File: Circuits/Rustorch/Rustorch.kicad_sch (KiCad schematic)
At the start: 57 parts, among them CN1 USB_C_Receptacle_USB2.0_16P, CN2 OLED_128x64_IIC, Q1 2SC1815, Q2 2SC1815, Q3 2SC1815, Q4 2SC1815, SW1 RESET, SW2 SW_UP, SW3 SW_LEFT, SW4 SW_RIGHT, SW5 SW_DOWN, SW6 SW_A, SW7 SW_B, SW8 SW_BOOT, SW9 SW_POWER (5P), U1 ESP32-C6-WROOM-1, U2 BA033CC0T, U3 OSL10561-L*, U4 OSL10561-L*, U5 OSL10561-L*, U6 OSL10561-L*

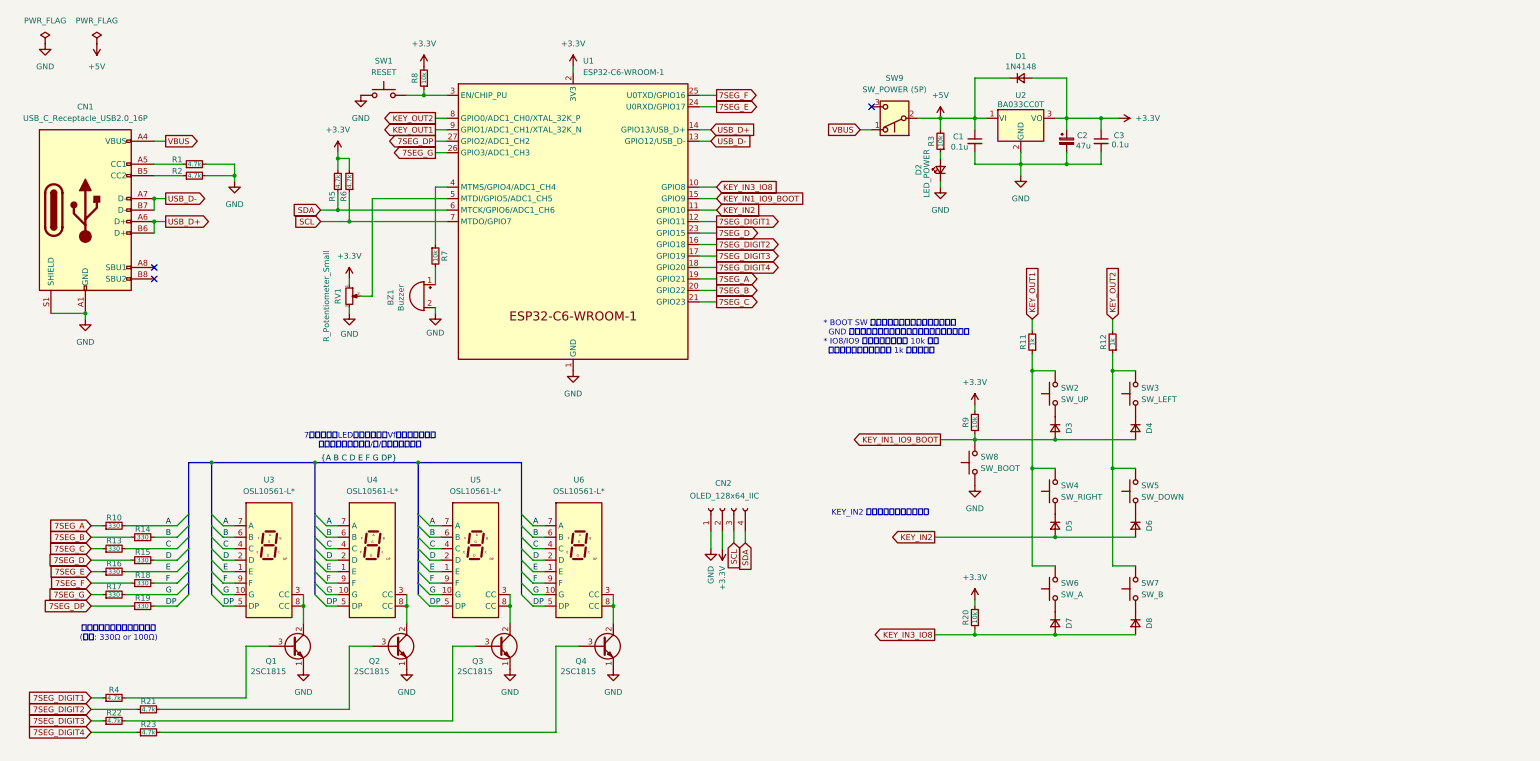
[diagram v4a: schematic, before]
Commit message: (Rustorch) 回路図修正 (部品番号の振り直し)
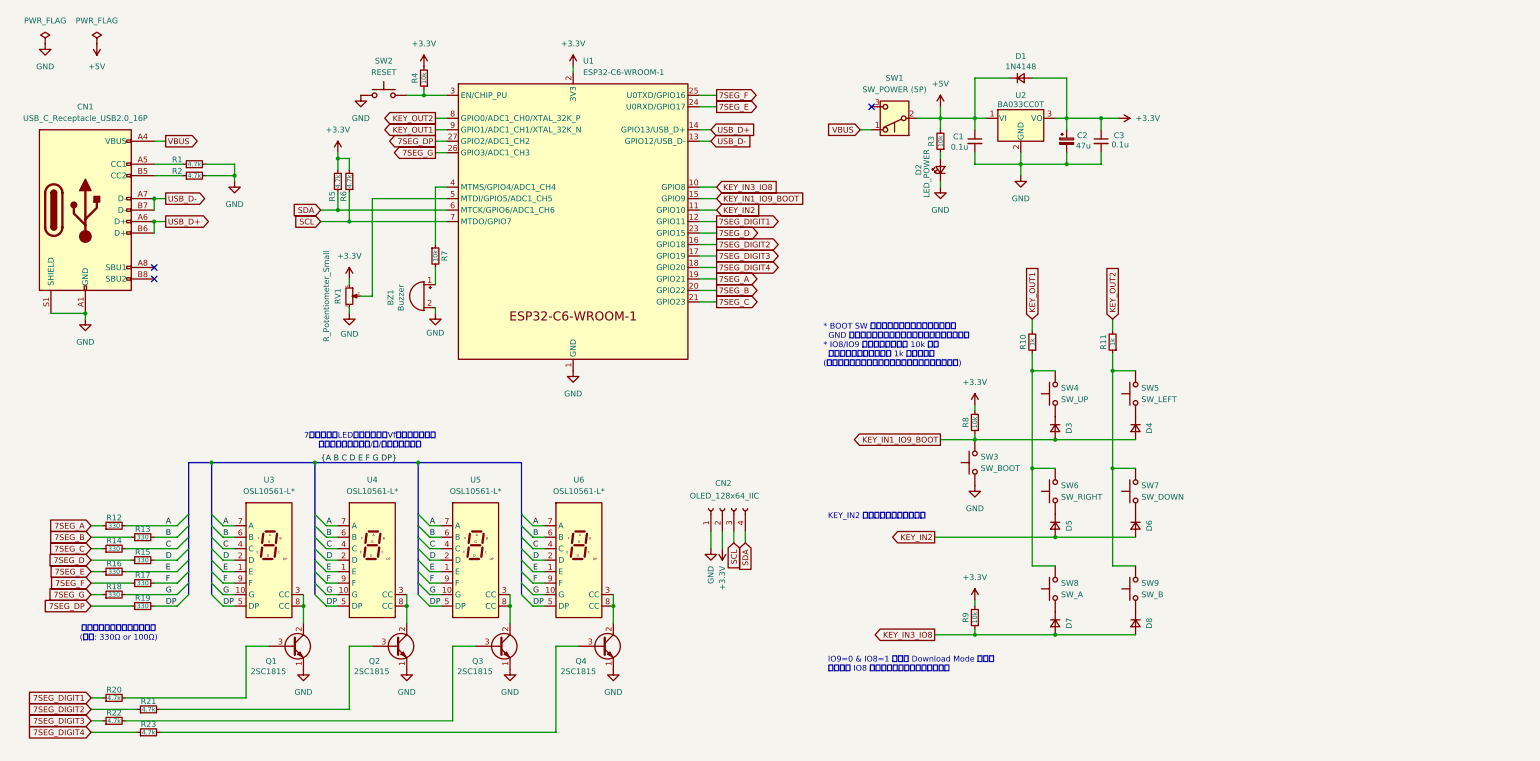
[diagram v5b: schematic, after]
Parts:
- renumbered R11 to R10, R12 to R11, R10 to R12, R14 to R13, R13 to R14, R18 to R17, R17 to R18, R4 to R20, R8 to R4, R9 to R8, R20 to R9, SW9 to SW1, SW1 to SW2, SW8 to SW3, SW2 to SW4, SW3 to SW5, SW4 to SW6, SW5 to SW7, SW6 to SW8, SW7 to SW9
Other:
- note added: "* BOOT SW 押下時にキースキャン用の出力が GND 直結になるのを防止する用に直列抵抗を入れる * IO8/IO9 のプルアップ抵抗 10k との 分圧を考えて直列抵抗は 1k にしておく (ダイオードがあるので不要かもしれないが念のため)"
- note added: "IO9=0 & IO8=1 の時に Download Mode になる このため IO8 にプルアップ抵抗を入れておく"
- note removed: "* BOOT SW 押下時にキースキャン用の出力が GND 直結になるのを防止する用に直列抵抗を入れる * IO8/IO9 のプルアップ抵抗 10k との 分圧を考えて直列抵抗は 1k にしておく"
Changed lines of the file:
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@@
 	(wire
 		(pts
+			(xy 224.79 39.37) (xy 224.79 41.91)
+		)
+		(stroke
+			(width 0)
+			(type default)
+		)
+	)
+	(wire
+		(pts
 			(xy 250.19 41.91) (xy 252.73 41.91)
 		)
@@
 	(text "KEY_IN2 は内蔵プルアップを使用"
 		(exclude_from_sim no)
-		(at 200.66 129.286 0)
+		(at 199.898 130.048 0)
+		(effects
+			(font
+				(face "Meiryo UI")
+				(size 1.27 1.27)
+			)
+			(justify left)
+		)
+	)
+	(text "IO9=0 & IO8=1 の時に Download Mode になる\nこのため IO8 にプルアップ抵抗を入れておく"
+		(exclude_from_sim no)
+		(at 199.898 162.814 0)
 		(effects
 			(font
@@
 		)
 	)
-	(text "* BOOT SW 押下時にキースキャン用の出力が\n  GND 直結になるのを防止する用に直列抵抗を入れる\n* IO8/IO9 のプルアップ抵抗 10k との\n  分圧を考えて直列抵抗は 1k にしておく"
+	(text "* BOOT SW 押下時にキースキャン用の出力が\n  GND 直結になるのを防止する用に直列抵抗を入れる\n* IO8/IO9 のプルアップ抵抗 10k との\n  分圧を考えて直列抵抗は 1k にしておく\n(ダイオードがあるので不要かもしれないが念のため)"
 		(exclude_from_sim no)
-		(at 198.882 90.424 0)
+		(at 198.882 92.202 0)
 		(effects
 			(font
@@
 	(symbol
 		(lib_id "power:+5V")
-		(at 224.79 41.91 0)
+		(at 224.79 39.37 0)
 		(unit 1)
 		(exclude_from_sim no)
@@
 		(fields_autoplaced yes)
 		(property "Reference" "#PWR020"
-			(at 224.79 45.72 0)
+			(at 224.79 43.18 0)
 			(effects
 				(font
@@
 		)
 		(property "Value" "+5V"
-			(at 224.79 36.83 0)
+			(at 224.79 34.29 0)
 			(effects
 				(font
@@
 		)
 		(property "Footprint" ""
-			(at 224.79 41.91 0)
+			(at 224.79 39.37 0)
 			(effects
 				(font
@@
 		)
 		(property "Datasheet" ""
-			(at 224.79 41.91 0)
+			(at 224.79 39.37 0)
 			(effects
 				(font
@@
 		)
 		(property "Description" "Power symbol creates a global label with name \"+5V\""
-			(at 224.79 41.91 0)
+			(at 224.79 39.37 0)
 			(effects
 				(font
@@
 		(on_board yes)
 		(dnp no)
-		(property "Reference" "R12"
+		(property "Reference" "R11"
 			(at 260.858 91.44 90)
 			(effects
@@
 			(project "Rustorch"
 				(path "/3b188497-bb0d-4776-a9fa-7cb2b780d2ff"
-					(reference "R12")
+					(reference "R11")
 					(unit 1)
 				)
@@
 		(dnp no)
 		(fields_autoplaced yes)
-		(property "Reference" "SW9"
+		(property "Reference" "SW1"
 			(at 214.63 33.02 0)
 			(effects
@@
 			(project ""
 				(path "/3b188497-bb0d-4776-a9fa-7cb2b780d2ff"
-					(reference "SW9")
+					(reference "SW1")
 					(unit 1)
 				)
@@
 		(on_board yes)
 		(dnp no)
-		(property "Reference" "R17"
+		(property "Reference" "R18"
 			(at 41.91 145.542 90)
 			(effects
@@
 			(project "Rustorch"
 				(path "/3b188497-bb0d-4776-a9fa-7cb2b780d2ff"
-					(reference "R17")
+					(reference "R18")
 					(unit 1)
 				)
@@
 		(on_board yes)
 		(dnp no)
-		(property "Reference" "R18"
+		(property "Reference" "R17"
 			(at 48.26 143.002 90)
 			(effects
@@
 			(project "Rustorch"
 				(path "/3b188497-bb0d-4776-a9fa-7cb2b780d2ff"
-					(reference "R18")
+					(reference "R17")
 					(unit 1)
 				)
@@
 		(dnp no)
 		(fields_autoplaced yes)
-		(property "Reference" "SW4"
+		(property "Reference" "SW6"
 			(at 251.46 123.1899 90)
 			(effects
@@
 			(project "Rustorch"
 				(path "/3b188497-bb0d-4776-a9fa-7cb2b780d2ff"
-					(reference "SW4")
+					(reference "SW6")
 					(unit 1)
 				)
@@
 		(on_board yes)
 		(dnp no)
-		(property "Reference" "R9"
+		(property "Reference" "R8"
 			(at 230.378 109.22 90)
 			(effects
@@
 			(project "Rustorch"
 				(path "/3b188497-bb0d-4776-a9fa-7cb2b780d2ff"
-					(reference "R9")
+					(reference "R8")
 					(unit 1)
 				)
@@
 		(dnp no)
 		(fields_autoplaced yes)
-		(property "Reference" "SW8"
+		(property "Reference" "SW3"
 			(at 233.68 116.8399 90)
 			(effects
@@
 			(project "Rustorch"
 				(path "/3b188497-bb0d-4776-a9fa-7cb2b780d2ff"
-					(reference "SW8")
+					(reference "SW3")
 					(unit 1)
 				)
@@
 		(on_board yes)
 		(dnp no)
-		(property "Reference" "R11"
+		(property "Reference" "R10"
 			(at 243.078 91.44 90)
 			(effects
@@
 			(project "Rustorch"
 				(path "/3b188497-bb0d-4776-a9fa-7cb2b780d2ff"
-					(reference "R11")
+					(reference "R10")
 					(unit 1)
 				)
@@
 		(dnp no)
 		(fields_autoplaced yes)
-		(property "Reference" "SW6"
+		(property "Reference" "SW8"
 			(at 251.46 144.7799 90)
 			(effects
@@
 			(project "Rustorch"
 				(path "/3b188497-bb0d-4776-a9fa-7cb2b780d2ff"
-					(reference "SW6")
+					(reference "SW8")
 					(unit 1)
 				)
@@
 		(on_board yes)
 		(dnp no)
-		(property "Reference" "R10"
+		(property "Reference" "R12"
 			(at 41.91 130.302 90)
 			(effects
@@
 			(project "Rustorch"
 				(path "/3b188497-bb0d-4776-a9fa-7cb2b780d2ff"
-					(reference "R10")
+					(reference "R12")
 					(unit 1)
 				)
@@
 		(dnp no)
 		(fields_autoplaced yes)
-		(property "Reference" "SW3"
+		(property "Reference" "SW5"
 			(at 269.24 101.5999 90)
 			(effects
@@
 			(project "Rustorch"
 				(path "/3b188497-bb0d-4776-a9fa-7cb2b780d2ff"
-					(reference "SW3")
+					(reference "SW5")
 					(unit 1)
 				)
@@
 		(dnp no)
 		(fields_autoplaced yes)
-		(property "Reference" "SW1"
+		(property "Reference" "SW2"
 			(at 101.6 29.21 0)
 			(effects
@@
 			(project ""
 				(path "/3b188497-bb0d-4776-a9fa-7cb2b780d2ff"
-					(reference "SW1")
+					(reference "SW2")
 					(unit 1)
 				)
@@
 		(on_board yes)
 		(dnp no)
-		(property "Reference" "R20"
+		(property "Reference" "R9"
 			(at 230.378 152.4 90)
 			(effects
@@
 			(project "Rustorch"
 				(path "/3b188497-bb0d-4776-a9fa-7cb2b780d2ff"
-					(reference "R20")
+					(reference "R9")
 					(unit 1)
 				)
@@
 		(on_board yes)
 		(dnp no)
-		(property "Reference" "R14"
+		(property "Reference" "R13"
 			(at 48.26 132.842 90)
 			(effects
@@
 			(project "Rustorch"
 				(path "/3b188497-bb0d-4776-a9fa-7cb2b780d2ff"
-					(reference "R14")
+					(reference "R13")
 					(unit 1)
 				)
@@
 		(on_board yes)
 		(dnp no)
-		(property "Reference" "R4"
+		(property "Reference" "R20"
 			(at 41.91 168.402 90)
 			(effects
@@
 			(project "Rustorch"
 				(path "/3b188497-bb0d-4776-a9fa-7cb2b780d2ff"
-					(reference "R4")
+					(reference "R20")
 					(unit 1)
 				)
@@
 		(on_board yes)
 		(dnp no)
-		(property "Reference" "R13"
+		(property "Reference" "R14"
 			(at 41.91 135.382 90)
 			(effects
@@
 			(project "Rustorch"
 				(path "/3b188497-bb0d-4776-a9fa-7cb2b780d2ff"
-					(reference "R13")
+					(reference "R14")
 					(unit 1)
 				)
@@
 		(dnp no)
 		(fields_autoplaced yes)
-		(property "Reference" "SW7"
+		(property "Reference" "SW9"
 			(at 269.24 144.7799 90)
 			(effects
@@
 			(project "Rustorch"
 				(path "/3b188497-bb0d-4776-a9fa-7cb2b780d2ff"
-					(reference "SW7")
+					(reference "SW9")
 					(unit 1)
 				)
@@
 		(dnp no)
 		(fields_autoplaced yes)
-		(property "Reference" "SW2"
+		(property "Reference" "SW4"
 			(at 251.46 101.5999 90)
 			(effects
@@
 			(project ""
 				(path "/3b188497-bb0d-4776-a9fa-7cb2b780d2ff"
-					(reference "SW2")
+					(reference "SW4")
 					(unit 1)
 				)
@@
 		(on_board yes)
 		(dnp no)
-		(property "Reference" "R8"
+		(property "Reference" "R4"
 			(at 108.458 33.02 90)
 			(effects
@@
 			(project "Rustorch"
 				(path "/3b188497-bb0d-4776-a9fa-7cb2b780d2ff"
-					(reference "R8")
+					(reference "R4")
 					(unit 1)
 				)
@@
 		(dnp no)
 		(fields_autoplaced yes)
-		(property "Reference" "SW5"
+		(property "Reference" "SW7"
 			(at 269.24 123.1899 90)
 			(effects
@@
 			(project "Rustorch"
 				(path "/3b188497-bb0d-4776-a9fa-7cb2b780d2ff"
-					(reference "SW5")
+					(reference "SW7")
 					(unit 1)
 				)

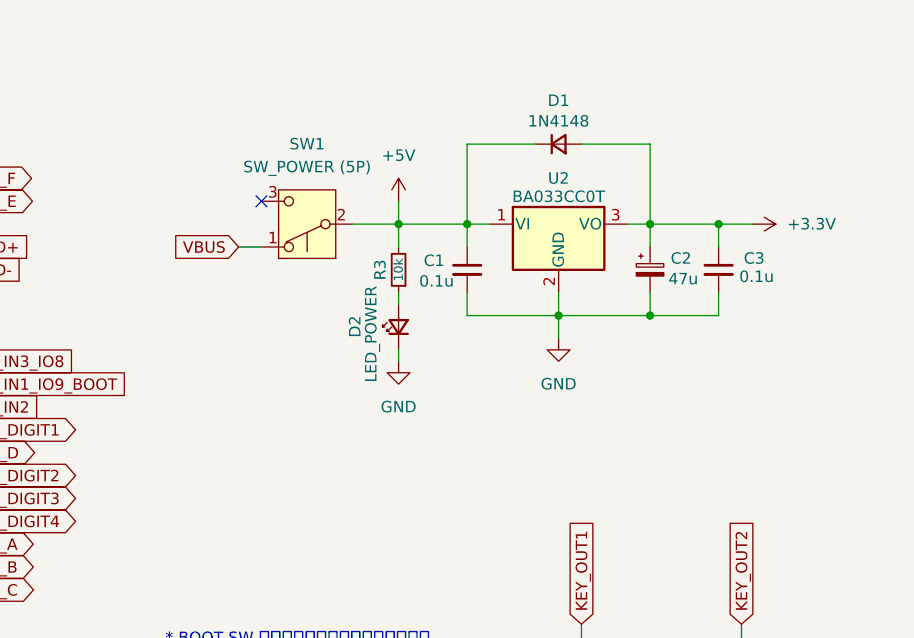
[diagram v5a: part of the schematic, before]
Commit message: (Rustorch) 回路図修正 (三端子レギュレータ VI のコンデンサを電解に修正)
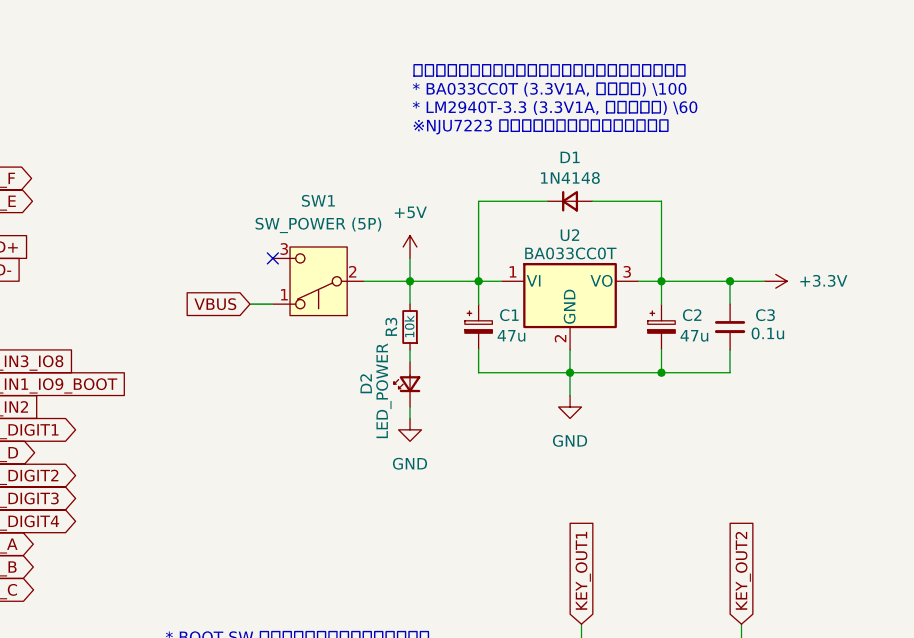
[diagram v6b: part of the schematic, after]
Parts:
- removed C1: 0.1u, symbol Device:C_Small
- added C1: 47u, Capacitor_THT:CP_Radial_D5.0mm_P2.50mm, symbol Device:C_Polarized_Small
- BZ1: footprint (none) -> extsui:Buzzer_PS_RP2_C13_40
- C2: footprint (none) -> Capacitor_THT:CP_Radial_D5.0mm_P2.50mm
- C3: footprint (none) -> Capacitor_THT:C_Disc_D3.0mm_W2.0mm_P2.50mm
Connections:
- net +5V: now also C1.1
- net GND: now also C1.2
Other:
- note added: "三端子レギュレータは以下のいずれかを使用する予定 * BA033CC0T (3.3V1A, モールド) \100 * LM2940T-3.3 (3.3V1A, 非モールド) \60 ※NJU7223 はピン配置が異なるので使用不可"
- moved on the sheet: C2, C3, D1, D2, R3, SW1, U2
